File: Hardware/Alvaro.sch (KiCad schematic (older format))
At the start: 24 parts, among them J2 01x02, J3 01x12, J4 01x12, J5 01x05, P1 USB_C_Receptacle_USB2.0, U1 ATmega32U4, X1 16MHz

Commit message: SOD323 schottky switched to SOD123
Bigger means less heat issues
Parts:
- D1: footprint Diode_SMD:D_SOD-323 -> Diode_SMD:D_SOD-123
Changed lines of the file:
@@
 F 0 "D1" H 3250 1400 50  0000 C CNN
 F 1 "D_Schottky" H 3250 1200 50  0000 C CNN
-F 2 "Diode_SMD:D_SOD-323" H 3250 1300 50  0001 C CNN
+F 2 "Diode_SMD:D_SOD-123" H 3250 1300 50  0001 C CNN
 F 3 "" H 3250 1300 50  0001 C CNN
 	1    3250 1300

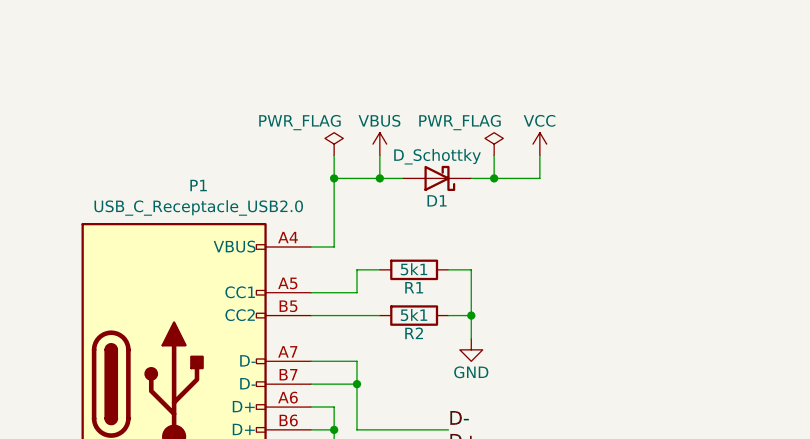
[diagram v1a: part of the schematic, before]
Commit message: Updated to V1.1
Added 1206 500mA polyfuse to design, rerouted and moved parts, changed renders
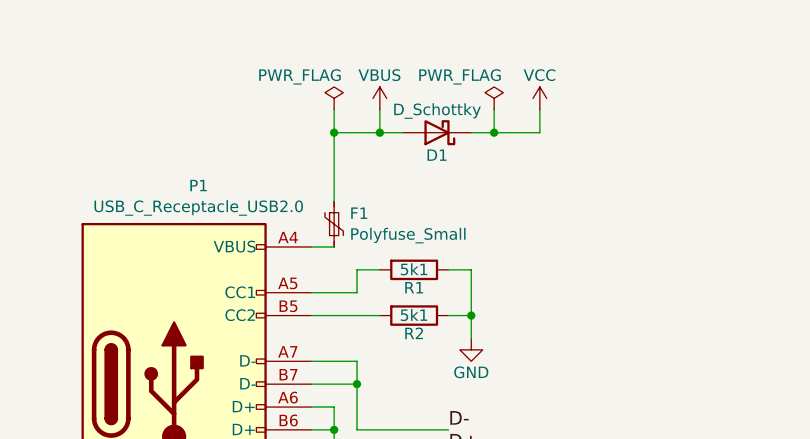
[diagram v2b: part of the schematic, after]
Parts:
- added F1: Polyfuse_Small, Fuse:Fuse_1206_3216Metric, symbol Device:Polyfuse_Small
- P1: footprint Alvaro:USB-C-C168688 -> Alvaro:USB-C_C168688
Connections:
- net VBUS: now also F1.1; no longer P1.A4 (VBUS), P1.A9 (VBUS), P1.B4 (VBUS), P1.B9 (VBUS)
- new net: F1.2, P1.A4 (VBUS), P1.A9 (VBUS), P1.B4 (VBUS), P1.B9 (VBUS)
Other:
- moved on the sheet: D1
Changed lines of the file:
@@
 L power:PWR_FLAG #FLG03
 U 1 1 5A285693
-P 2800 1200
-F 0 "#FLG03" H 2800 1275 50  0001 C CNN
-F 1 "PWR_FLAG" H 2650 1350 50  0000 C CNN
-F 2 "" H 2800 1200 50  0001 C CNN
-F 3 "" H 2800 1200 50  0001 C CNN
-	1    2800 1200
+P 2800 1000
+F 0 "#FLG03" H 2800 1075 50  0001 C CNN
+F 1 "PWR_FLAG" H 2650 1150 50  0000 C CNN
+F 2 "" H 2800 1000 50  0001 C CNN
+F 3 "" H 2800 1000 50  0001 C CNN
+	1    2800 1000
 	1    0    0    -1
 $EndComp
@@
 	2800 1600 2700 1600
 Wire Wire Line
-	2800 1200 2800 1300
-Connection ~ 2800 1300
+	2800 1000 2800 1100
+Connection ~ 2800 1100
 Wire Wire Line
 	2700 1900 3000 1900
@@
 Connection ~ 3400 1900
 Wire Wire Line
-	3000 1300 3000 1200
+	3000 1100 3000 1000
 Wire Wire Line
 	4150 3250 4250 3250
@@
 L power:VBUS #PWR016
 U 1 1 5A78C3BD
-P 3000 1200
-F 0 "#PWR016" H 3000 1050 50  0001 C CNN
-F 1 "VBUS" H 3000 1350 50  0000 C CNN
-F 2 "" H 3000 1200 50  0001 C CNN
-F 3 "" H 3000 1200 50  0001 C CNN
-	1    3000 1200
+P 3000 1000
+F 0 "#PWR016" H 3000 850 50  0001 C CNN
+F 1 "VBUS" H 3000 1150 50  0000 C CNN
+F 2 "" H 3000 1000 50  0001 C CNN
+F 3 "" H 3000 1000 50  0001 C CNN
+	1    3000 1000
 	1    0    0    -1
 $EndComp
@@
 L Device:D_Schottky D1
 U 1 1 5A78E24C
-P 3250 1300
-F 0 "D1" H 3250 1400 50  0000 C CNN
-F 1 "D_Schottky" H 3250 1200 50  0000 C CNN
-F 2 "Diode_SMD:D_SOD-123" H 3250 1300 50  0001 C CNN
-F 3 "" H 3250 1300 50  0001 C CNN
-	1    3250 1300
+P 3250 1100
+F 0 "D1" H 3250 1200 50  0000 C CNN
+F 1 "D_Schottky" H 3250 1000 50  0000 C CNN
+F 2 "Diode_SMD:D_SOD-123" H 3250 1100 50  0001 C CNN
+F 3 "" H 3250 1100 50  0001 C CNN
+	1    3250 1100
 	-1   0    0    1
 $EndComp
-Connection ~ 3000 1300
-Wire Wire Line
-	3400 1300 3500 1300
-Wire Wire Line
-	3700 1300 3700 1200
+Connection ~ 3000 1100
+Wire Wire Line
+	3400 1100 3500 1100
+Wire Wire Line
+	3700 1100 3700 1000
 $Comp
 L power:VCC #PWR019
 U 1 1 5A78E470
-P 3700 1200
-F 0 "#PWR019" H 3700 1050 50  0001 C CNN
-F 1 "VCC" H 3700 1350 50  0000 C CNN
-F 2 "" H 3700 1200 50  0001 C CNN
-F 3 "" H 3700 1200 50  0001 C CNN
-	1    3700 1200
+P 3700 1000
+F 0 "#PWR019" H 3700 850 50  0001 C CNN
+F 1 "VCC" H 3700 1150 50  0000 C CNN
+F 2 "" H 3700 1000 50  0001 C CNN
+F 3 "" H 3700 1000 50  0001 C CNN
+	1    3700 1000
 	1    0    0    -1
 $EndComp
@@
 L power:PWR_FLAG #FLG020
 U 1 1 5A79EAD6
-P 3500 1200
-F 0 "#FLG020" H 3500 1275 50  0001 C CNN
-F 1 "PWR_FLAG" H 3350 1350 50  0000 C CNN
-F 2 "" H 3500 1200 50  0001 C CNN
-F 3 "" H 3500 1200 50  0001 C CNN
-	1    3500 1200
-	1    0    0    -1
-$EndComp
-Wire Wire Line
-	3500 1200 3500 1300
-Connection ~ 3500 1300
+P 3500 1000
+F 0 "#FLG020" H 3500 1075 50  0001 C CNN
+F 1 "PWR_FLAG" H 3350 1150 50  0000 C CNN
+F 2 "" H 3500 1000 50  0001 C CNN
+F 3 "" H 3500 1000 50  0001 C CNN
+	1    3500 1000
+	1    0    0    -1
+$EndComp
+Wire Wire Line
+	3500 1000 3500 1100
+Connection ~ 3500 1100
 $Comp
 L power:VBUS #PWR021
@@
 $EndComp
 Wire Wire Line
-	2800 1300 3000 1300
+	2800 1100 3000 1100
 Wire Wire Line
 	3400 1900 3400 2000
@@
 	5100 900  5400 900
 Wire Wire Line
-	3000 1300 3100 1300
-Wire Wire Line
-	3500 1300 3700 1300
+	3000 1100 3100 1100
+Wire Wire Line
+	3500 1100 3700 1100
 Wire Wire Line
 	6300 900  6600 900
@@
 Connection ~ 6600 1400
 Wire Wire Line
-	2800 1300 2800 1600
+	2800 1100 2800 1400
 Wire Wire Line
 	2100 3200 2200 3200
@@
 F 0 "P1" H 2207 3067 50  0000 C CNN
 F 1 "USB_C_Receptacle_USB2.0" H 2207 2976 50  0000 C CNN
-F 2 "Alvaro:USB-C-C168688" H 2250 2200 50  0001 C CNN
+F 2 "Alvaro:USB-C_C168688" H 2250 2200 50  0001 C CNN
 F 3 "https://www.usb.org/sites/default/files/documents/usb_type-c.zip" H 2250 2200 50  0001 C CNN
 	1    2100 2200
@@
 	0    1    1    0
 $EndComp
+$Comp
+L Device:Polyfuse_Small F1
+U 1 1 5F86C93F
+P 2800 1500
+F 0 "F1" H 2868 1546 50  0000 L CNN
+F 1 "Polyfuse_Small" H 2868 1455 50  0000 L CNN
+F 2 "Fuse:Fuse_1206_3216Metric" H 2850 1300 50  0001 L CNN
+F 3 "~" H 2800 1500 50  0001 C CNN
+	1    2800 1500
+	1    0    0    -1
+$EndComp
 $EndSCHEMATC

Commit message: Updated to 1.3
Added 0603 power indicator LED, changed R6 from 10k to 1k LED resistor.
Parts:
- added D2: LED, LED_SMD:LED_0603_1608Metric, symbol Device:LED
- R6: value 10k -> 1k
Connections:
- net GND: now also D2.1 (K); no longer R6.1
- new net: D2.2 (A), R6.1
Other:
- moved on the sheet: R6
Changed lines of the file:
@@
 L Device:R R6
 U 1 1 5CBBA935
-P 6900 1150
-F 0 "R6" V 6980 1150 50  0000 C CNN
-F 1 "10k" V 6900 1150 50  0000 C CNN
-F 2 "Resistor_SMD:R_0603_1608Metric" V 6830 1150 50  0001 C CNN
-F 3 "" H 6900 1150 50  0001 C CNN
-	1    6900 1150
-	-1   0    0    1
-$EndComp
-Wire Wire Line
-	6900 1000 6900 900
-Wire Wire Line
-	6900 900  6600 900
-Connection ~ 6600 900
-Wire Wire Line
-	6900 1300 6900 1400
-Wire Wire Line
-	6900 1400 6600 1400
-Connection ~ 6600 1400
+P 6750 900
+F 0 "R6" V 6830 900 50  0000 C CNN
+F 1 "1k" V 6750 900 50  0000 C CNN
+F 2 "Resistor_SMD:R_0603_1608Metric" V 6680 900 50  0001 C CNN
+F 3 "" H 6750 900 50  0001 C CNN
+	1    6750 900
+	0    1    -1   0
+$EndComp
 Wire Wire Line
 	2800 1100 2800 1400
@@
 	1    0    0    -1
 $EndComp
+$Comp
+L Device:LED D2
+U 1 1 5FA0B438
+P 6750 1400
+F 0 "D2" H 6750 1200 50  0000 C CNN
+F 1 "LED" H 6750 1300 50  0000 C CNN
+F 2 "LED_SMD:LED_0603_1608Metric" H 6750 1400 50  0001 C CNN
+F 3 "~" H 6750 1400 50  0001 C CNN
+	1    6750 1400
+	1    0    0    -1
+$EndComp
+Wire Wire Line
+	6900 900  6900 1400
+Connection ~ 6600 900
+Connection ~ 6600 1400
 $EndSCHEMATC

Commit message: Updated to V1.4.
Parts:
- P1: footprint Alvaro:USB-C_C168688 -> Alvaro:USB-C-C168688
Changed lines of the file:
@@
 F 0 "P1" H 2207 3067 50  0000 C CNN
 F 1 "USB_C_Receptacle_USB2.0" H 2207 2976 50  0000 C CNN
-F 2 "Alvaro:USB-C_C168688" H 2250 2200 50  0001 C CNN
+F 2 "Alvaro:USB-C-C168688" H 2250 2200 50  0001 C CNN
 F 3 "https://www.usb.org/sites/default/files/documents/usb_type-c.zip" H 2250 2200 50  0001 C CNN
 	1    2100 2200

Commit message: Updated to V1.5
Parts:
- added JP1: RAW, Jumper:SolderJumper-2_P1.3mm_Open_Pad1.0x1.5mm, symbol Device:Jumper_NO_Small
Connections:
- net VBUS: now also JP1.1; no longer J3.1 (Pin_1)
- new net: J3.1 (Pin_1), JP1.2
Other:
- note removed: "Released under the Creative Commons Attribution Share-Alike 4.0 License\nhttps://creativecommons.org/licenses/by-sa/4.0/\n\nOriginal Arduino Mini Design by Team Arduino\nArduino Pro Mini Design by Spark Fun Electronics\nPro Micro Design by Spark Fun Electronics\nGoldfish Design by dr_derivative"
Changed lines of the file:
@@
 encoding utf-8
 Sheet 1 1
-Title "Goldfish"
-Date "2017-12-20"
-Rev "C"
+Title "Alvaro"
+Date "2020-12-03"
+Rev "V1.5"
 Comp ""
 Comment1 ""
@@
 	5000 900  5000 800
 Connection ~ 5100 900
-Text Notes 700  7600 0    60   ~ 0
-Released under the Creative Commons Attribution Share-Alike 4.0 License\nhttps://creativecommons.org/licenses/by-sa/4.0/\n\nOriginal Arduino Mini Design by Team Arduino\nArduino Pro Mini Design by Spark Fun Electronics\nPro Micro Design by Spark Fun Electronics\nGoldfish Design by dr_derivative
 $Comp
 L power:VBUS #PWR016
@@
 	0    -1   -1   0
 $EndComp
-Wire Wire Line
-	5050 3250 5350 3250
 Wire Wire Line
 	6000 900  6000 1000
@@
 Connection ~ 6600 900
 Connection ~ 6600 1400
+$Comp
+L Device:Jumper_NO_Small JP1
+U 1 1 5FC92C0A
+P 5200 3250
+F 0 "JP1" H 5200 3435 50  0000 C CNN
+F 1 "RAW" H 5200 3344 50  0000 C CNN
+F 2 "Jumper:SolderJumper-2_P1.3mm_Open_Pad1.0x1.5mm" H 5200 3250 50  0001 C CNN
+F 3 "~" H 5200 3250 50  0001 C CNN
+	1    5200 3250
+	1    0    0    -1
+$EndComp
+Wire Wire Line
+	5350 3250 5300 3250
+Wire Wire Line
+	5100 3250 5050 3250
 $EndSCHEMATC
